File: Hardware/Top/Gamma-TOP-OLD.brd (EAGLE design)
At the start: 38 x 38 mm, 63 parts, among them SW1 SWITCH.MOM, SW2 SWITCH.MOM, U1 FT231XS, U3 NRF52832_MODULE_MDBT42, U5 FT24C64A, Y1 32.768kHz

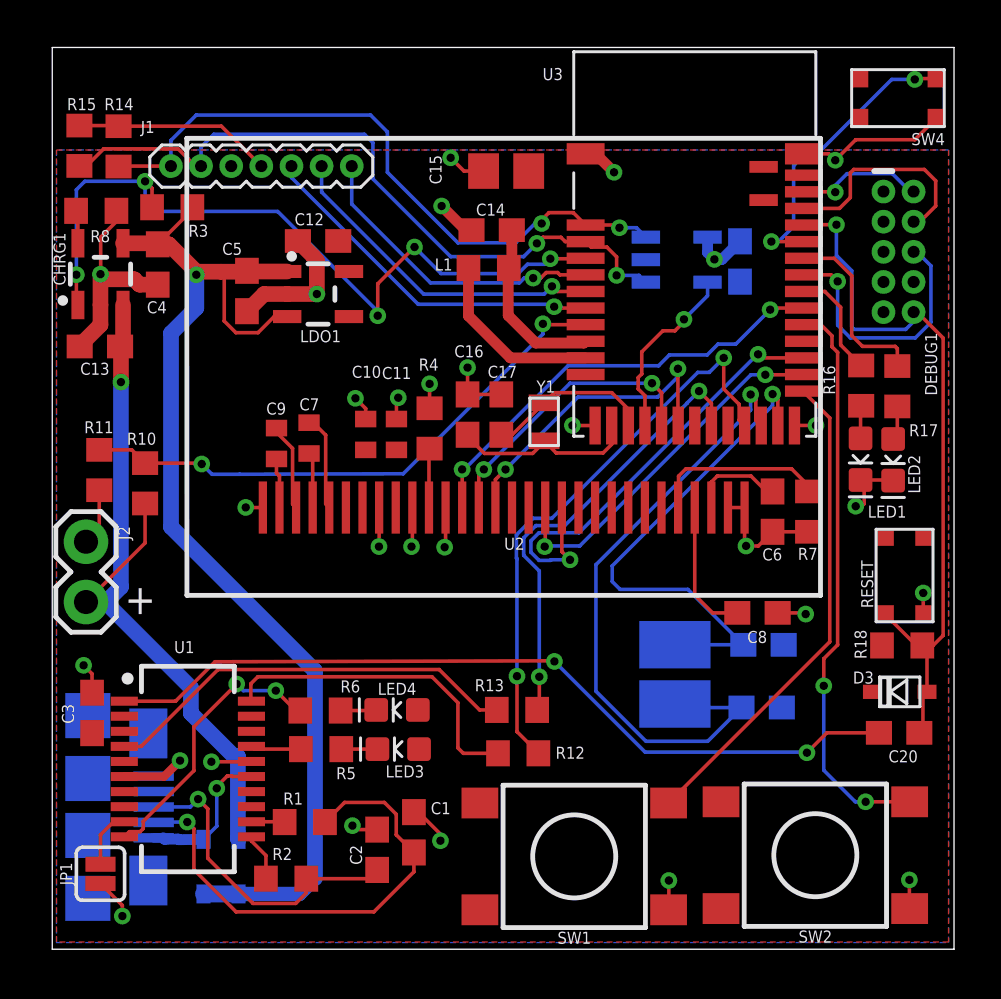
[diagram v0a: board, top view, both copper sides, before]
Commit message: Updated file names and completed preliminary BOM for each board
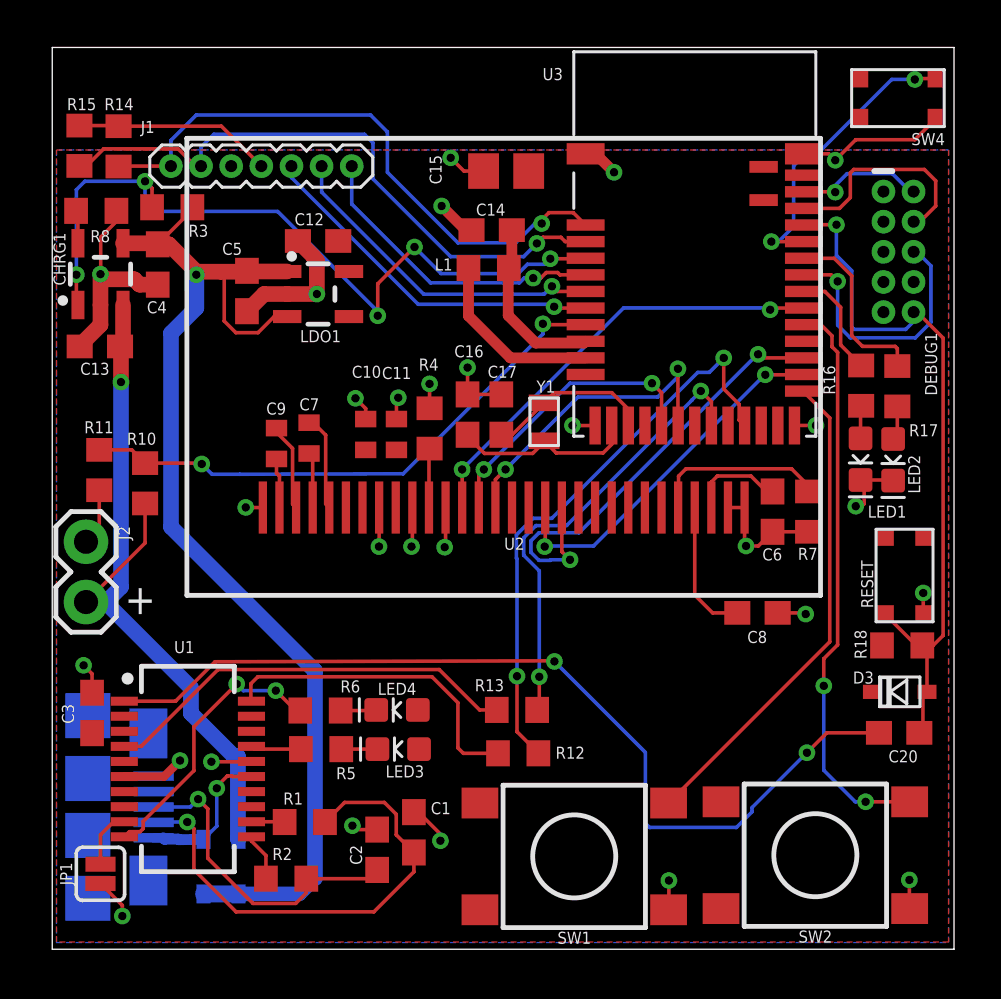
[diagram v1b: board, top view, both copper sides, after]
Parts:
- removed C18, C21: 120p, LinnesLab-Passives:C0603
- removed C19: 100n, LinnesLab-Passives:C0603
- removed NFCANTENNA: 2.1 uH, NFC-Antenna:1462360151
- removed U5: FT24C64A, LinnesLab-DigitalIC:SOT23-5
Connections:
- removed net WP: U3.15, U5.5
- net 3.3V: no longer C19.1, U5.4
- net GND: no longer C18.2, C19.2, C21.2, U5.2
- net P0.09/NFC1: no longer C18.1, NFCANTENNA.NFC1
- net P0.10/NFC2: no longer C21.1, NFCANTENNA.NFC2
- net SCL: no longer U5.1
- net SDA: no longer U5.3
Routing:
- net P0.09/NFC1: track 27.2 -> 0.00 mm, vias 1 -> 0
- net P0.10/NFC2: track 21.6 -> 0.00 mm, vias 1 -> 0
- net WP: track 7.67 -> 0.00 mm, vias 1 -> 0
- net DTR: track 34.4 -> 38.9 mm
- net SCL: track 30.1 -> 26.4 mm, vias 2 -> 1
- net SDA: track 28.0 -> 25.3 mm, vias 2 -> 1
- net 3.3V: track 10.8 -> 8.37 mm, vias 1 -> 0
